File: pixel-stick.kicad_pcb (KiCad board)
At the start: 2 copper layers, 16.5 x 37.1 mm, 15 parts, among them J2 WS28**, U1 AZ1117-3.3, U2 ESP-01v090, U3 SN74LVC1T45DBV, U4 RT9361A

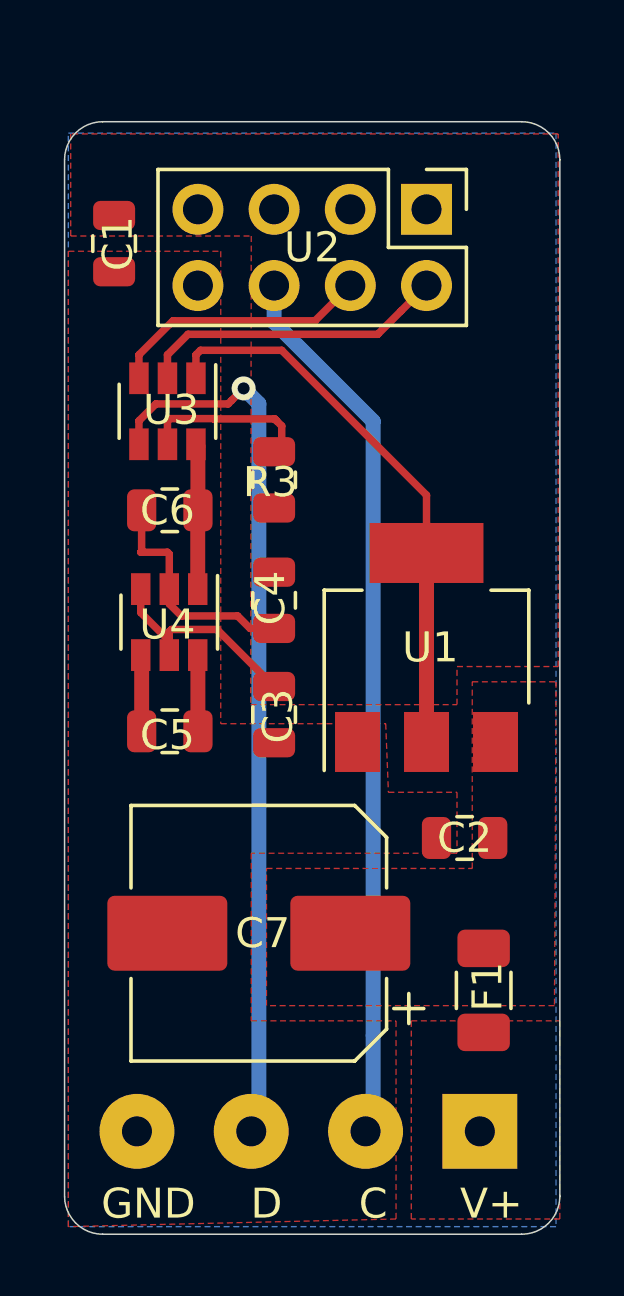
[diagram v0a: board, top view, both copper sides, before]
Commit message: removed paralell and adjacent caps
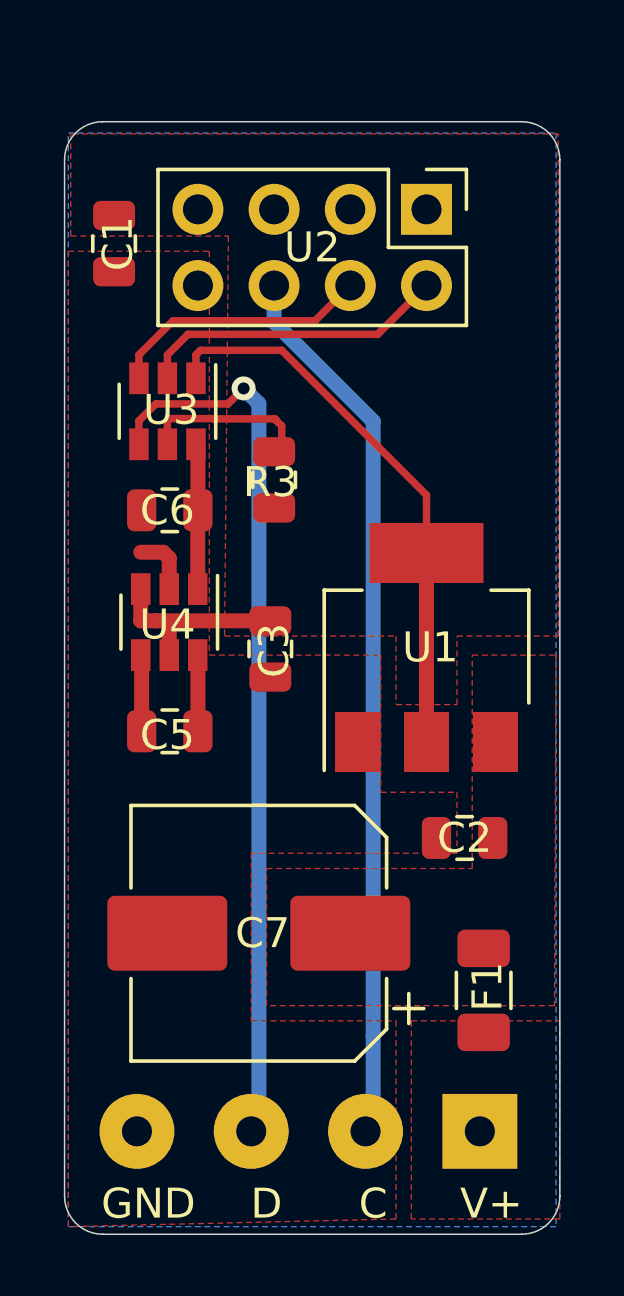
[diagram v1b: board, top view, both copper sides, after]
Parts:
- removed C4: 10µF, Capacitor_SMD:C_0805_2012Metric
- moved C3 2.19 mm to (49.4, 71.2)
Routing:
- net GND: track 18.3 -> 12.4 mm
- net +3V3: track 26.5 -> 25.3 mm
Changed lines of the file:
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@@
     (thickness 1.6)
     (drawings 13)
-    (tracks 62)
+    (tracks 51)
     (zones 0)
-    (modules 15)
+    (modules 14)
     (nets 16)
   )
@@
   )
   (setup
-    (last_trace_width 0.25)
+    (last_trace_width 0.5)
     (user_trace_width 0.5)
     (user_trace_width 1)
@@
     (mod_text_size 1 1)
     (mod_text_width 0.15)
-    (pad_size 1.524 1.524)
-    (pad_drill 0.762)
+    (pad_size 1 1)
+    (pad_drill 0)
     (pad_to_mask_clearance 0.051)
     (solder_mask_min_width 0.25)
@@
   )
   (module Capacitor_SMD:C_0805_2012Metric (layer F.Cu)
-    (at 49.53 69.5475 270)
-    (descr "Capacitor SMD 0805 (2012 Metric), square (rectangular) end terminal, IPC_7351 nominal, (Body size source: https://docs.google.com/spreadsheets/d/1BsfQQcO9C6DZCsRaXUlFlo91Tg2WpOkGARC1WS5S8t0/edit?usp=sharing), generated with kicad-footprint-generator")
-    (tags capacitor)
-    (attr smd)
-    (fp_text reference C4 (at -0.0785 0.127 90) (layer F.SilkS)
-      (effects (font (size 1 1) (thickness 0.15)))
-    )
-    (fp_text value 10µF (at 0 1.65 90) (layer F.Fab)
-      (effects (font (size 1 1) (thickness 0.15)))
-    )
-    (fp_text user %R (at 0 0 90) (layer F.Fab)
-      (effects (font (size 0.5 0.5) (thickness 0.08)))
-    )
-    (fp_line (start 1.68 0.95) (end -1.68 0.95) (layer F.CrtYd) (width 0.05))
-    (fp_line (start 1.68 -0.95) (end 1.68 0.95) (layer F.CrtYd) (width 0.05))
-    (fp_line (start -1.68 -0.95) (end 1.68 -0.95) (layer F.CrtYd) (width 0.05))
-    (fp_line (start -1.68 0.95) (end -1.68 -0.95) (layer F.CrtYd) (width 0.05))
-    (fp_line (start -0.258578 0.71) (end 0.258578 0.71) (layer F.SilkS) (width 0.12))
-    (fp_line (start -0.258578 -0.71) (end 0.258578 -0.71) (layer F.SilkS) (width 0.12))
-    (fp_line (start 1 0.6) (end -1 0.6) (layer F.Fab) (width 0.1))
-    (fp_line (start 1 -0.6) (end 1 0.6) (layer F.Fab) (width 0.1))
-    (fp_line (start -1 -0.6) (end 1 -0.6) (layer F.Fab) (width 0.1))
-    (fp_line (start -1 0.6) (end -1 -0.6) (layer F.Fab) (width 0.1))
-    (pad 2 smd roundrect (at 0.9375 0 270) (size 0.975 1.4) (layers F.Cu F.Paste F.Mask) (roundrect_rratio 0.25)
-      (net 1 GND))
-    (pad 1 smd roundrect (at -0.9375 0 270) (size 0.975 1.4) (layers F.Cu F.Paste F.Mask) (roundrect_rratio 0.25)
-      (net 2 +3V3))
-    (model ${KISYS3DMOD}/Capacitor_SMD.3dshapes/C_0805_2012Metric.wrl
-      (at (xyz 0 0 0))
-      (scale (xyz 1 1 1))
-      (rotate (xyz 0 0 0))
-    )
-  )
-  (module Capacitor_SMD:C_0805_2012Metric (layer F.Cu)
-    (at 49.53 73.3575 270)
+    (at 49.403 71.1685 270)
     (descr "Capacitor SMD 0805 (2012 Metric), square (rectangular) end terminal, IPC_7351 nominal, (Body size source: https://docs.google.com/spreadsheets/d/1BsfQQcO9C6DZCsRaXUlFlo91Tg2WpOkGARC1WS5S8t0/edit?usp=sharing), generated with kicad-footprint-generator")
     (tags capacitor)
@@
   (segment (start 52.984989 60.680011) (end 53.760001 59.904999) (width 0.25) (layer F.Cu) (net 1))
   (segment (start 45.974 62.146) (end 45.974 61.366) (width 0.25) (layer F.Cu) (net 1))
-  (segment (start 48.73 70.485) (end 49.53 70.485) (width 0.25) (layer F.Cu) (net 1))
-  (segment (start 48.313989 70.068989) (end 48.73 70.485) (width 0.25) (layer F.Cu) (net 1))
-  (segment (start 46.439987 70.068989) (end 48.313989 70.068989) (width 0.25) (layer F.Cu) (net 1))
-  (segment (start 46.035 69.664002) (end 46.439987 70.068989) (width 0.25) (layer F.Cu) (net 1))
-  (segment (start 46.035 69.174) (end 46.035 69.664002) (width 0.25) (layer F.Cu) (net 1))
-  (segment (start 46.035 69.174) (end 46.035 68.006) (width 0.25) (layer F.Cu) (net 1))
-  (segment (start 46.035 68.006) (end 45.974 67.945) (width 0.25) (layer F.Cu) (net 1))
-  (segment (start 45.974 67.945) (end 45.085 67.945) (width 0.25) (layer F.Cu) (net 1))
-  (segment (start 45.115 67.915) (end 45.115 66.548) (width 0.25) (layer F.Cu) (net 1))
-  (segment (start 45.085 67.945) (end 45.115 67.915) (width 0.25) (layer F.Cu) (net 1))
-  (segment (start 45.085 69.954) (end 46.035 70.904) (width 0.25) (layer F.Cu) (net 2))
-  (segment (start 46.035 70.904) (end 46.035 71.374) (width 0.25) (layer F.Cu) (net 2))
-  (segment (start 45.085 69.174) (end 45.085 69.954) (width 0.25) (layer F.Cu) (net 2))
+  (segment (start 46.035 68.144) (end 45.836 67.945) (width 0.5) (layer F.Cu) (net 1))
+  (segment (start 46.035 69.174) (end 46.035 68.144) (width 0.5) (layer F.Cu) (net 1))
+  (segment (start 45.836 67.945) (end 45.085 67.945) (width 0.5) (layer F.Cu) (net 1))
   (segment (start 52.04 56.485) (end 52.07 56.515) (width 0.25) (layer B.Cu) (net 2))
   (segment (start 54.61 74.27) (end 54.61 67.97) (width 0.5) (layer F.Cu) (net 2))
@@
   (segment (start 54.61 66.04) (end 54.61 67.97) (width 0.25) (layer F.Cu) (net 2))
   (segment (start 49.784 61.214) (end 54.61 66.04) (width 0.25) (layer F.Cu) (net 2))
-  (segment (start 48.973763 71.863763) (end 49.53 72.42) (width 0.25) (layer F.Cu) (net 2))
-  (segment (start 47.628999 70.518999) (end 48.973763 71.863763) (width 0.25) (layer F.Cu) (net 2))
-  (segment (start 46.035 70.594) (end 46.110001 70.518999) (width 0.25) (layer F.Cu) (net 2))
-  (segment (start 46.110001 70.518999) (end 47.628999 70.518999) (width 0.25) (layer F.Cu) (net 2))
-  (segment (start 46.035 71.374) (end 46.035 70.594) (width 0.25) (layer F.Cu) (net 2))
+  (segment (start 45.085 69.174) (end 45.085 70.231) (width 0.5) (layer F.Cu) (net 2))
+  (segment (start 46.035 71.374) (end 46.035 70.292) (width 0.5) (layer F.Cu) (net 2))
+  (segment (start 45.593 70.231) (end 49.403 70.231) (width 0.5) (layer F.Cu) (net 2))
+  (segment (start 45.085 70.231) (end 45.593 70.231) (width 0.5) (layer F.Cu) (net 2))
   (segment (start 45.115 71.404) (end 45.085 71.374) (width 0.5) (layer F.Cu) (net 4))
   (segment (start 45.115 73.914) (end 45.115 71.404) (width 0.5) (layer F.Cu) (net 4))
@@
     (polygon
       (pts
-        (xy 42.672 57.912) (xy 47.752 57.912) (xy 47.752 73.66) (xy 53.25 73.66) (xy 53.34 75.946)
+        (xy 42.672 57.912) (xy 47.371 57.912) (xy 47.371 71.374) (xy 53.086 71.374) (xy 53.086 75.946)
         (xy 55.626 75.946) (xy 55.626 77.978) (xy 48.768 77.978) (xy 48.768 83.566) (xy 53.594 83.566)
         (xy 53.594 90.17) (xy 42.672 90.424)
@@
     (polygon
       (pts
-        (xy 56.134 72.263) (xy 58.928 72.263) (xy 58.875 83.058) (xy 49.276 83.058) (xy 49.276 78.486)
+        (xy 56.134 71.374) (xy 58.928 71.374) (xy 58.875 83.058) (xy 49.276 83.058) (xy 49.276 78.486)
         (xy 56.134 78.486)
-      )
-    )
-  )
-  (zone (net 2) (net_name +3V3) (layer F.Cu) (hatch edge 0.508)
-    (connect_pads (clearance 0.508))
-    (min_thickness 0.254)
-    (fill yes (arc_segments 32) (thermal_gap 0.508) (thermal_bridge_width 0.508))
-    (polygon
-      (pts
-        (xy 48.75 73.025) (xy 55.626 73.025) (xy 55.626 71.755) (xy 59 71.755) (xy 59 54)
-        (xy 42.75 54) (xy 42.75 57.404) (xy 48.768 57.404)
       )
     )
@@
       )
     )
+  )
+  (zone (net 2) (net_name +3V3) (layer F.Cu) (hatch edge 0.508)
+    (connect_pads (clearance 0.508))
+    (min_thickness 0.254)
+    (fill yes (arc_segments 32) (thermal_gap 0.508) (thermal_bridge_width 0.508))
+    (polygon
+      (pts
+        (xy 47.879 70.739) (xy 53.594 70.739) (xy 53.594 73.025) (xy 55.626 73.025) (xy 55.626 70.739)
+        (xy 59 70.739) (xy 59 54) (xy 42.75 54) (xy 42.75 57.404) (xy 48.006 57.404)
+      )
+    )

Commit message: add power led
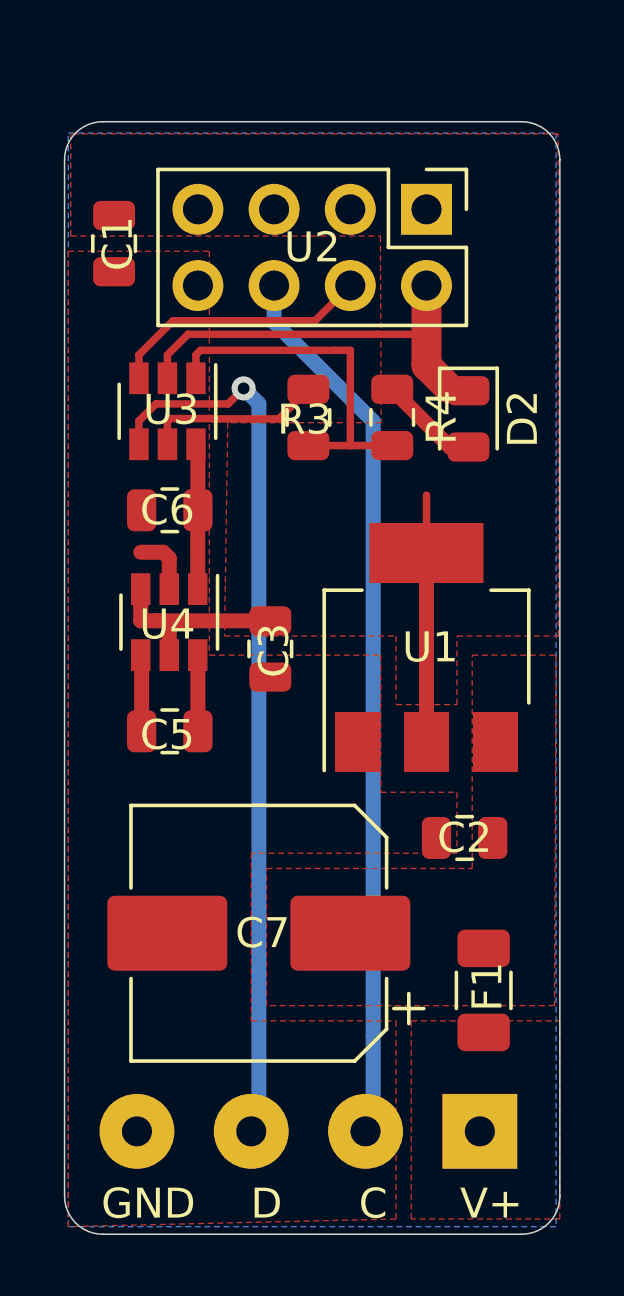
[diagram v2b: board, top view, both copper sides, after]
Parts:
- added D2: LED, LED_SMD:LED_0805_2012Metric, F.Cu at (56.0, 63.5)
- added R4: 10k, Resistor_SMD:R_0805_2012Metric, F.Cu at (53.5, 63.5)
- moved R3 2.37 mm to (50.7, 63.5)
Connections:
- J2 pad 2: /CLOCK -> /DATA
- J2 pad 3: /DATA -> /CLOCK
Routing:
- net Net-(D2-Pad2): track 0.00 -> 3.34 mm
- net GND: track 12.4 -> 15.7 mm
- net +3V3: track 25.3 -> 26.7 mm

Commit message: fix drc errors
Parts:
- R4: value 10k -> 120
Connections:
- J2 pad 2: /DATA -> /CLOCK
- J2 pad 3: /CLOCK -> /DATA
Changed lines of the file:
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@@
   )
   (setup
-    (last_trace_width 0.25)
+    (last_trace_width 1)
     (user_trace_width 0.5)
     (user_trace_width 1)
@@
       (effects (font (size 1 1) (thickness 0.15)))
     )
-    (fp_text value 10k (at 0 1.65 90) (layer F.Fab)
+    (fp_text value 120 (at 0 1.65 90) (layer F.Fab)
       (effects (font (size 1 1) (thickness 0.15)))
     )
@@
       (net 1 GND))
     (pad 3 thru_hole circle (at 7.62 0 180) (size 2.49936 2.49936) (drill 1.00076) (layers *.Cu *.Mask)
+      (net 11 /DATA))
+    (pad 2 thru_hole circle (at 3.81 0 180) (size 2.49936 2.49936) (drill 1.00076) (layers *.Cu *.Mask)
       (net 10 /CLOCK))
-    (pad 2 thru_hole circle (at 3.81 0 180) (size 2.49936 2.49936) (drill 1.00076) (layers *.Cu *.Mask)
-      (net 11 /DATA))
     (pad 1 thru_hole rect (at 0 0 180) (size 2.49936 2.49936) (drill 1.00076) (layers *.Cu *.Mask)
       (net 8 /VIN))
@@
   (segment (start 54.460011 60.680011) (end 54.61 60.83) (width 0.25) (layer F.Cu) (net 1))
   (segment (start 52.984989 60.680011) (end 54.460011 60.680011) (width 0.25) (layer F.Cu) (net 1))
-  (segment (start 54.61 61.722) (end 55.372 62.484) (width 1) (layer F.Cu) (net 1))
-  (segment (start 54.61 59.055) (end 54.61 61.722) (width 1) (layer F.Cu) (net 1))
+  (segment (start 54.61 61.1655) (end 56.007 62.5625) (width 1) (layer F.Cu) (net 1))
+  (segment (start 54.61 59.055) (end 54.61 61.1655) (width 1) (layer F.Cu) (net 1))
   (segment (start 52.04 56.485) (end 52.07 56.515) (width 0.25) (layer B.Cu) (net 2))
   (segment (start 54.61 74.27) (end 54.61 67.97) (width 0.5) (layer F.Cu) (net 2))
